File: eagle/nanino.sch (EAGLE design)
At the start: 19 parts, among them IC1 ATMEGA328P-20, Q1 16MHz

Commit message: improved routing
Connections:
- net GND renamed GND1
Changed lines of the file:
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@@
 </segment>
 </net>
-<net name="GND" class="0">
+<net name="GND1" class="0">
 <segment>
 <pinref part="GND1" gate="1" pin="GND"/>

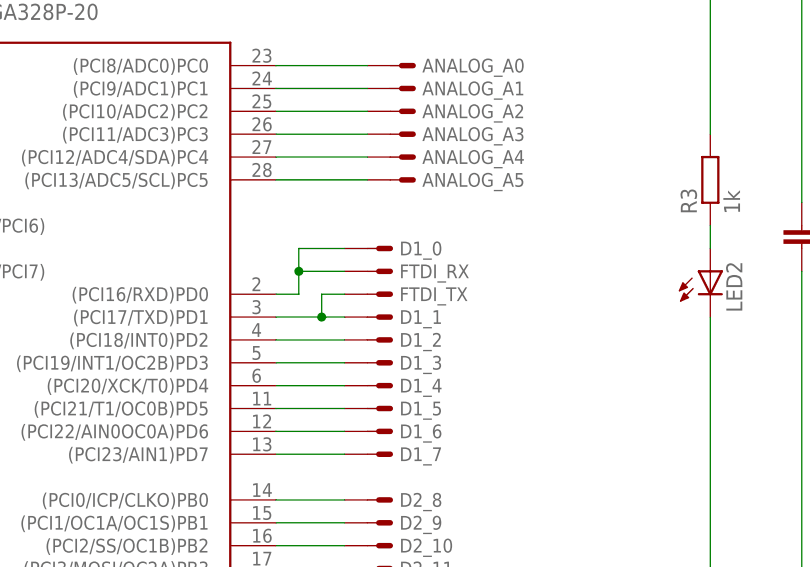
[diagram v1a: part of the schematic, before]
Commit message: Version 1.1 - FTDI Rx/Tx corrected, bigger solder pads
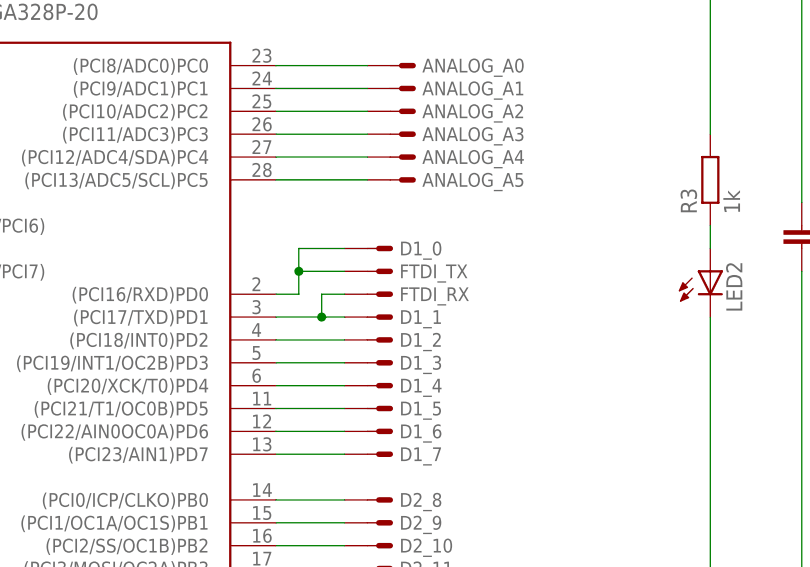
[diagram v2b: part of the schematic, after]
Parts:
- C1, C2, C3, C4: device rcl:C-EU025-025X050 -> rc:C-EU025-025X050
- C5: device elkos:CPOL-EUE2.5-5 -> elkos:CPOL-EUE2.5-5-L-12
- C6: device rcl:C-EU025-025X050 -> rc:C-EU050-025X075
- LED1, LED2: device SparkFun:LED3MM -> leds:LED3MM
- Q1: device SparkFun:CRYSTALHC49US -> crystals:CRYSTALHC49U-V
- R1, R2, R3: device rcl:R-EU_0207/10 -> rc:R-EU_0207/10
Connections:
- net GND1 renamed GND
- net N$1: now also FTDI_TX.S; no longer FTDI_RX.S
- net N$2: now also FTDI_RX.S; no longer FTDI_TX.S
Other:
- moved on the sheet: FTDI_RX, FTDI_TX
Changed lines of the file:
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@@
 <grid distance="0.1" unitdist="inch" unit="inch" style="lines" multiple="1" display="no" altdistance="0.01" altunitdist="inch" altunit="inch"/>
 <layers>
-<layer number="1" name="Top" color="4" fill="1" visible="no" active="no"/>
-<layer number="16" name="Bottom" color="1" fill="1" visible="no" active="no"/>
-<layer number="17" name="Pads" color="2" fill="1" visible="no" active="no"/>
-<layer number="18" name="Vias" color="2" fill="1" visible="no" active="no"/>
-<layer number="19" name="Unrouted" color="6" fill="1" visible="no" active="no"/>
-<layer number="20" name="Dimension" color="15" fill="1" visible="no" active="no"/>
-<layer number="21" name="tPlace" color="7" fill="1" visible="no" active="no"/>
-<layer number="22" name="bPlace" color="7" fill="1" visible="no" active="no"/>
-<layer number="23" name="tOrigins" color="15" fill="1" visible="no" active="no"/>
-<layer number="24" name="bOrigins" color="15" fill="1" visible="no" active="no"/>
-<layer number="25" name="tNames" color="7" fill="1" visible="no" active="no"/>
-<layer number="26" name="bNames" color="7" fill="1" visible="no" active="no"/>
-<layer number="27" name="tValues" color="7" fill="1" visible="no" active="no"/>
-<layer number="28" name="bValues" color="7" fill="1" visible="no" active="no"/>
+<layer number="1" name="Top" color="4" fill="1" visible="yes" active="no"/>
+<layer number="16" name="Bottom" color="1" fill="1" visible="yes" active="no"/>
+<layer number="17" name="Pads" color="2" fill="1" visible="yes" active="no"/>
+<layer number="18" name="Vias" color="2" fill="1" visible="yes" active="no"/>
+<layer number="19" name="Unrouted" color="6" fill="1" visible="yes" active="no"/>
+<layer number="20" name="Dimension" color="15" fill="1" visible="yes" active="no"/>
+<layer number="21" name="tPlace" color="7" fill="1" visible="yes" active="no"/>
+<layer number="22" name="bPlace" color="7" fill="1" visible="yes" active="no"/>
+<layer number="23" name="tOrigins" color="15" fill="1" visible="yes" active="no"/>
+<layer number="24" name="bOrigins" color="15" fill="1" visible="yes" active="no"/>
+<layer number="25" name="tNames" color="7" fill="1" visible="yes" active="no"/>
+<layer number="26" name="bNames" color="7" fill="1" visible="yes" active="no"/>
+<layer number="27" name="tValues" color="7" fill="1" visible="yes" active="no"/>
+<layer number="28" name="bValues" color="7" fill="1" visible="yes" active="no"/>
 <layer number="29" name="tStop" color="7" fill="3" visible="no" active="no"/>
 <layer number="30" name="bStop" color="7" fill="6" visible="no" active="no"/>
@@
 <layer number="35" name="tGlue" color="7" fill="4" visible="no" active="no"/>
 <layer number="36" name="bGlue" color="7" fill="5" visible="no" active="no"/>
-<layer number="37" name="tTest" color="7" fill="1" visible="no" active="no"/>
-<layer number="38" name="bTest" color="7" fill="1" visible="no" active="no"/>
+<layer number="37" name="tTest" color="7" fill="1" visible="yes" active="no"/>
+<layer number="38" name="bTest" color="7" fill="1" visible="yes" active="no"/>
 <layer number="39" name="tKeepout" color="4" fill="11" visible="no" active="no"/>
 <layer number="40" name="bKeepout" color="1" fill="11" visible="no" active="no"/>
@@
 <layer number="44" name="Drills" color="7" fill="1" visible="no" active="no"/>
 <layer number="45" name="Holes" color="7" fill="1" visible="no" active="no"/>
-<layer number="46" name="Milling" color="3" fill="1" visible="no" active="no"/>
-<layer number="47" name="Measures" color="7" fill="1" visible="no" active="no"/>
-<layer number="48" name="Document" color="7" fill="1" visible="no" active="no"/>
-<layer number="49" name="Reference" color="7" fill="1" visible="no" active="no"/>
-<layer number="50" name="dxf" color="7" fill="1" visible="no" active="no"/>
-<layer number="51" name="tDocu" color="7" fill="1" visible="no" active="no"/>
-<layer number="52" name="bDocu" color="7" fill="1" visible="no" active="no"/>
-<layer number="53" name="tGND_GNDA" color="7" fill="9" visible="no" active="no"/>
-<layer number="54" name="bGND_GNDA" color="1" fill="9" visible="no" active="no"/>
-<layer number="56" name="wert" color="7" fill="1" visible="no" active="no"/>
+<layer number="46" name="Milling" color="3" fill="1" visible="yes" active="no"/>
+<layer number="47" name="Measures" color="7" fill="1" visible="yes" active="no"/>
+<layer number="48" name="Document" color="7" fill="1" visible="yes" active="no"/>
+<layer number="49" name="Reference" color="7" fill="1" visible="yes" active="no"/>
+<layer number="50" name="dxf" color="7" fill="1" visible="yes" active="no"/>
+<layer number="51" name="tDocu" color="7" fill="1" visible="yes" active="no"/>
+<layer number="52" name="bDocu" color="7" fill="1" visible="yes" active="no"/>
+<layer number="53" name="tGND_GNDA" color="7" fill="9" visible="yes" active="no"/>
+<layer number="54" name="bGND_GNDA" color="1" fill="9" visible="yes" active="no"/>
+<layer number="56" name="wert" color="7" fill="1" visible="yes" active="no"/>
 <layer number="91" name="Nets" color="2" fill="1" visible="yes" active="yes"/>
 <layer number="92" name="Busses" color="1" fill="1" visible="yes" active="yes"/>
@@
 <part name="PWR_" library="arduino" deviceset="PINS_ARDUINO_PWR" device="1"/>
 <part name="FTDI_" library="arduino" deviceset="PINS_FTDI" device="1"/>
-<part name="R1" library="rcl" deviceset="R-EU_" device="0207/10" value="1k"/>
-<part name="LED1" library="SparkFun" deviceset="LED" device="3MM"/>
+<part name="R1" library="rc" deviceset="R-EU_" device="0207/10" value="1k"/>
+<part name="LED1" library="leds" deviceset="LED" device="3MM"/>
 <part name="S1" library="switch" deviceset="TASTER" device="" technology="4.3MM"/>
-<part name="R2" library="rcl" deviceset="R-EU_" device="0207/10" value="10k"/>
-<part name="C1" library="rcl" deviceset="C-EU" device="025-025X050" value="100n"/>
-<part name="Q1" library="SparkFun" deviceset="CRYSTAL" device="HC49US" value="16MHz"/>
-<part name="C2" library="rcl" deviceset="C-EU" device="025-025X050" value="20pF"/>
-<part name="C3" library="rcl" deviceset="C-EU" device="025-025X050" value="20pF"/>
-<part name="R3" library="rcl" deviceset="R-EU_" device="0207/10" value="1k"/>
-<part name="LED2" library="SparkFun" deviceset="LED" device="3MM"/>
+<part name="R2" library="rc" deviceset="R-EU_" device="0207/10" value="10k"/>
+<part name="C1" library="rc" deviceset="C-EU" device="025-025X050" value="100n"/>
+<part name="Q1" library="crystals" deviceset="CRYSTAL" device="HC49U-V" value="16MHz"/>
+<part name="C2" library="rc" deviceset="C-EU" device="025-025X050" value="20pF"/>
+<part name="C3" library="rc" deviceset="C-EU" device="025-025X050" value="20pF"/>
+<part name="R3" library="rc" deviceset="R-EU_" device="0207/10" value="1k"/>
+<part name="LED2" library="leds" deviceset="LED" device="3MM"/>
 <part name="P+1" library="supply1" deviceset="VCC" device=""/>
 <part name="GND1" library="supply1" deviceset="GND" device=""/>
-<part name="C4" library="rcl" deviceset="C-EU" device="025-025X050" value="100n"/>
-<part name="C5" library="elkos" deviceset="CPOL-EU" device="E2.5-5" value="1uF"/>
-<part name="C6" library="rcl" deviceset="C-EU" device="025-025X050" value="100n"/>
+<part name="C4" library="rc" deviceset="C-EU" device="025-025X050" value="100n"/>
+<part name="C5" library="elkos" deviceset="CPOL-EU" device="E2.5-5-L-12" value="1uF"/>
+<part name="C6" library="rc" deviceset="C-EU" device="050-025X075" value="100n"/>
 </parts>
 <sheets>
@@
 <instance part="FTDI_" gate="CTS" x="116.84" y="20.32"/>
 <instance part="FTDI_" gate="PWR" x="104.14" y="116.84"/>
-<instance part="FTDI_" gate="TX" x="99.06" y="71.12"/>
-<instance part="FTDI_" gate="RX" x="99.06" y="73.66"/>
+<instance part="FTDI_" gate="TX" x="99.06" y="73.66"/>
+<instance part="FTDI_" gate="RX" x="99.06" y="71.12"/>
 <instance part="D1_" gate="7" x="99.06" y="53.34"/>
 <instance part="D2_" gate="AREF" x="-12.7" y="88.9" rot="R180"/>
@@
 <wire x1="88.9" y1="73.66" x2="88.9" y2="76.2" width="0.1524" layer="91"/>
 <wire x1="88.9" y1="76.2" x2="93.98" y2="76.2" width="0.1524" layer="91"/>
-<pinref part="FTDI_" gate="RX" pin="S"/>
+<junction x="88.9" y="73.66"/>
+<pinref part="FTDI_" gate="TX" pin="S"/>
 <wire x1="93.98" y1="73.66" x2="88.9" y2="73.66" width="0.1524" layer="91"/>
-<junction x="88.9" y="73.66"/>
 </segment>
 </net>
@@
 <pinref part="D1_" gate="1" pin="S"/>
 <wire x1="86.36" y1="68.58" x2="91.44" y2="68.58" width="0.1524" layer="91"/>
-<pinref part="FTDI_" gate="TX" pin="S"/>
 <wire x1="91.44" y1="68.58" x2="93.98" y2="68.58" width="0.1524" layer="91"/>
-<wire x1="93.98" y1="71.12" x2="91.44" y2="71.12" width="0.1524" layer="91"/>
 <wire x1="91.44" y1="71.12" x2="91.44" y2="68.58" width="0.1524" layer="91"/>
 <junction x="91.44" y="68.58"/>
+<pinref part="FTDI_" gate="RX" pin="S"/>
+<wire x1="91.44" y1="71.12" x2="93.98" y2="71.12" width="0.1524" layer="91"/>
 </segment>
 </net>
@@
 </segment>
 </net>
-<net name="GND1" class="0">
+<net name="GND" class="0">
 <segment>
 <pinref part="GND1" gate="1" pin="GND"/>
